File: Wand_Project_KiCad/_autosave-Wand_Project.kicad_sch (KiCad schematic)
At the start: 13 parts, among them J1 USB_B_Micro, J2 Conn_01x04_Pin, SW1 SW_SPDT, U1 STM32F401RETx, U2 MPU-6050

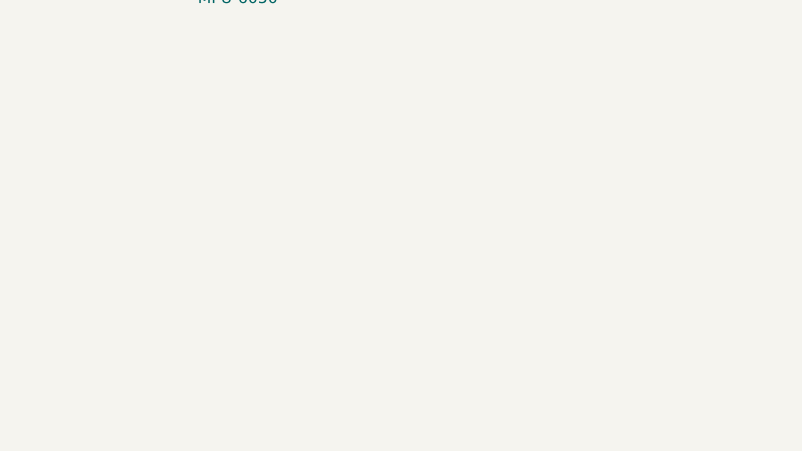
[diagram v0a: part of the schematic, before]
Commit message: rolling working, not time triggered
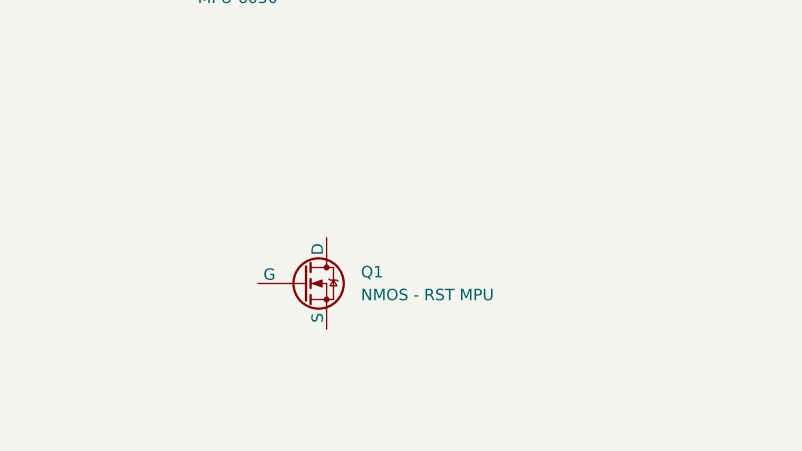
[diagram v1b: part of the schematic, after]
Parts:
- added Q1: NMOS - RST MPU, symbol Simulation_SPICE:NMOS
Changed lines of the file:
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@@
+	)
+	(symbol
+		(lib_id "Simulation_SPICE:NMOS")
+		(at 88.9 127 0)
+		(unit 1)
+		(exclude_from_sim no)
+		(in_bom yes)
+		(on_board yes)
+		(dnp no)
+		(fields_autoplaced yes)
+		(property "Reference" "Q1"
+			(at 95.25 125.7299 0)
+			(effects
+				(font
+					(size 1.27 1.27)
+				)
+				(justify left)
+			)
+		)
+		(property "Value" "NMOS - RST MPU"
+			(at 95.25 128.2699 0)
+			(effects
+				(font
+					(size 1.27 1.27)
+				)
+				(justify left)
+			)
+		)
+		(property "Footprint" ""
+			(at 93.98 124.46 0)
+			(effects
+				(font
+					(size 1.27 1.27)
+				)
+				(hide yes)
+			)
+		)
+		(property "Datasheet" "https://ngspice.sourceforge.io/docs/ngspice-html-manual/manual.xhtml#cha_MOSFETs"
+			(at 88.9 139.7 0)
+			(effects
+				(font
+					(size 1.27 1.27)
+				)
+				(hide yes)
+			)
+		)
+		(property "Description" "N-MOSFET transistor, drain/source/gate"
+			(at 88.9 127 0)
+			(effects
+				(font
+					(size 1.27 1.27)
+				)
+				(hide yes)
+			)
+		)
+		(property "Sim.Device" "NMOS"
+			(at 88.9 144.145 0)
+			(effects
+				(font
+					(size 1.27 1.27)
+				)
+				(hide yes)
+			)
+		)
+		(property "Sim.Type" "VDMOS"
+			(at 88.9 146.05 0)
+			(effects
+				(font
+					(size 1.27 1.27)
+				)
+				(hide yes)
+			)
+		)
+		(property "Sim.Pins" "1=D 2=G 3=S"
+			(at 88.9 142.24 0)
+			(effects
+				(font
+					(size 1.27 1.27)
+				)
+				(hide yes)
+			)
+		)
+		(pin "3"
+		)
+		(pin "1"
+		)
+		(pin "2"
+		)
+		(instances
+			(project ""
+				(path "/a9406932-9d61-4a8f-a88c-8d053bee548e"
+					(reference "Q1")
+					(unit 1)
+				)
+			)
+		)
 	)
 	(symbol
